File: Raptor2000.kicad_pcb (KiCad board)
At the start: 4 copper layers, 63.5 x 76.2 mm, 77 parts, among them J301 ET60T-000-3-08-D04-x-R1-S-x, J501 USB_B_Micro, SW401 RST_SW, U201 IS42S16400J-xC, U202 TC58CVG2S0HRAIG, U401 TM4C1294NCPDTGOOD, U501 FT232RL, Y401 Crystal_GND24, Y402 Crystal

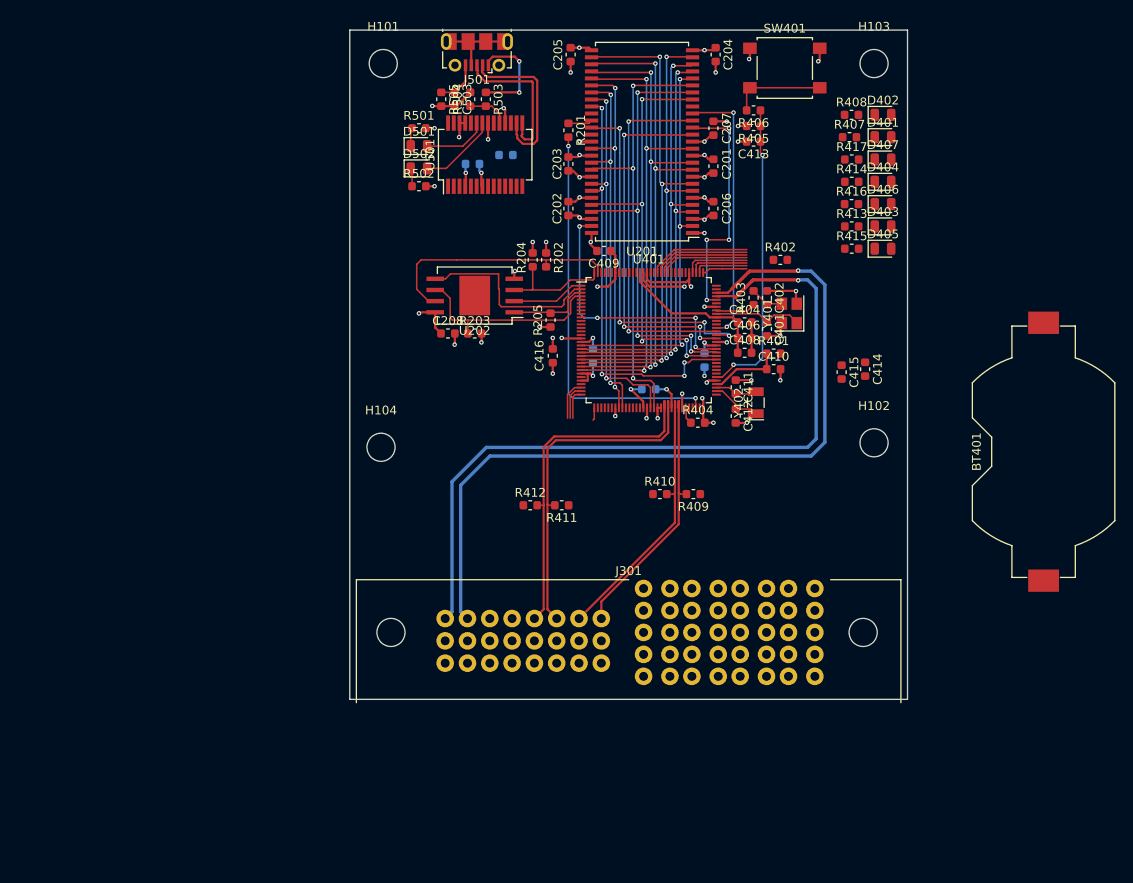
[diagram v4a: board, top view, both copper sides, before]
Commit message: replaced battery with ldo connected to external vbatt. Layout passes DRC
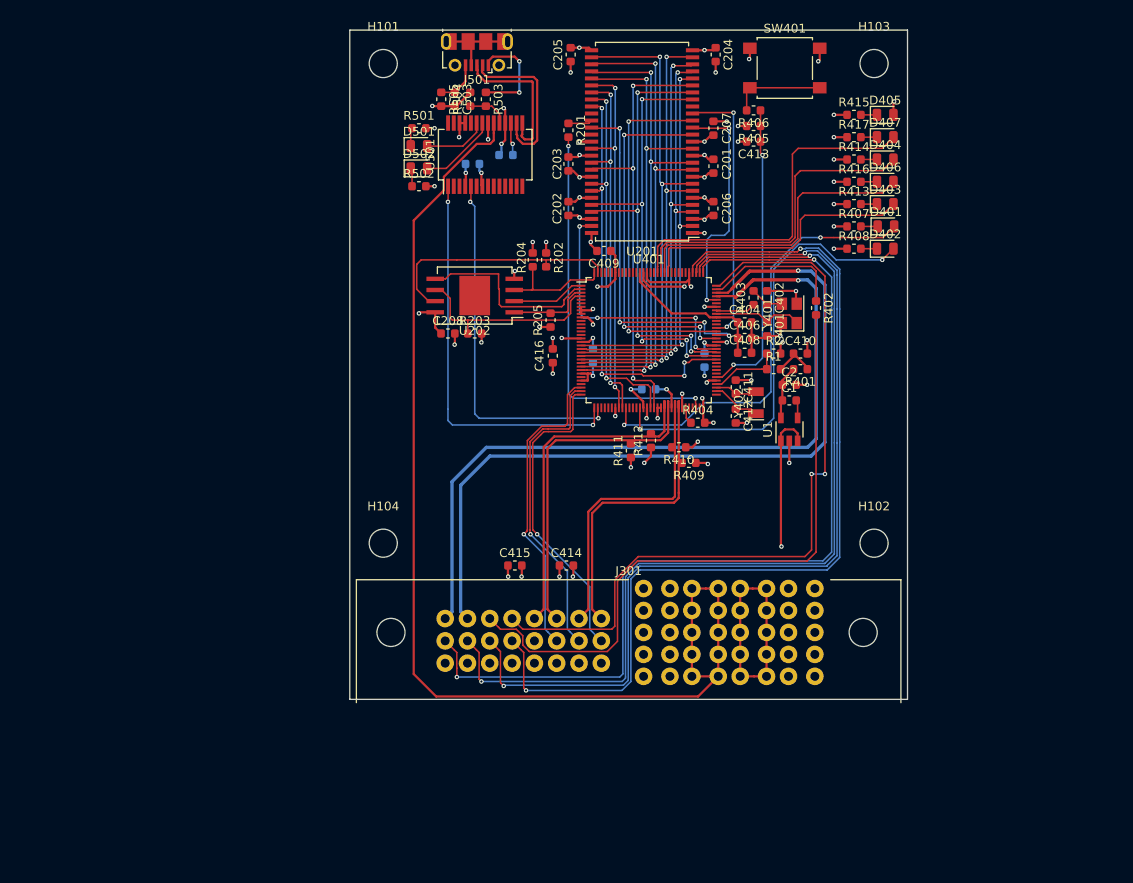
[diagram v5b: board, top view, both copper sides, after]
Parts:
- removed BT401: Battery_Cell, Battery:BatteryHolder_Keystone_1058_1x2032
- added C1: 0.1u, Capacitor_SMD:C_0603_1608Metric, F.Cu at (177.0, 93.0)
- added C2: 10u, Capacitor_SMD:C_0603_1608Metric, F.Cu at (177.0, 91.2)
- added R1: 0, Capacitor_SMD:C_0603_1608Metric, F.Cu at (175.3, 89.4)
- added R2: DNP, Capacitor_SMD:C_0603_1608Metric, F.Cu at (175.3, 87.6)
- added U1: LT1761-3, Package_TO_SOT_SMD:TSOT-23-5, F.Cu at (177.0, 96.3)
- moved C415 43.2 mm to (145.8, 111.8), turned to 0 degrees
- moved C414 40.7 mm to (151.7, 111.8), turned to 0 degrees
- moved R412 15.6 mm to (161.3, 97.5), turned to 90 degrees
- moved R408 15.2 mm to (184.4, 75.7)
- moved D402 15.2 mm to (188.0, 75.7)
- moved D405 15.2 mm to (188.0, 60.5)
- moved R415 15.2 mm to (184.4, 60.5)
- moved H102 11.4 mm to (186.7, 109.2)
- moved H104 10.9 mm to (130.8, 109.2)
- moved R407 10.2 mm to (184.4, 73.2)
- moved D401 10.2 mm to (188.0, 73.2)
- moved R411 10.0 mm to (159.0, 98.7), turned to 90 degrees
- moved R402 6.82 mm to (180.1, 82.4), turned to 270 degrees
- moved R410 5.75 mm to (164.5, 98.3), turned to 180 degrees
- moved R409 3.59 mm to (165.6, 100.1)
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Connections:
- U401 pad 68: /TM4C129/VBat -> /TM4C129/VBat_R
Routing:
- net +5V: track 0.00 -> 130.1 mm
- net /Connectors/JTAG_TDO: track 5.15 -> 107.6 mm, vias 0 -> 2
- net /Connectors/JTAG_TDI: track 6.10 -> 107.8 mm, vias 0 -> 2
- net /Connectors/JTAG_TMS: track 6.75 -> 107.7 mm, vias 0 -> 2
- net /Connectors/JTAG_TCK: track 7.40 -> 107.3 mm, vias 0 -> 2
- net /Connectors/USB_OTG_VBUS: track 0.00 -> 88.2 mm, vias 0 -> 2
- net /TM4C129/USB_ID: track 0.00 -> 75.0 mm
- net /TM4C129/ETH_LED1: track 0.00 -> 51.3 mm, vias 0 -> 2
- net /TM4C129/ETH_LED0: track 0.00 -> 50.4 mm, vias 0 -> 2
- net +BATT: track 0.00 -> 47.5 mm, vias 0 -> 1
- net /TM4C129/UART_DEBUG_RXD: track 1.47 -> 45.4 mm, vias 0 -> 2
- net /TM4C129/UART_DEBUG_TXD: track 0.00 -> 41.7 mm, vias 0 -> 2
- net /Connectors/~INHIBIT: track 3.47 -> 35.7 mm, vias 0 -> 1
- net /Connectors/~ENABLE: track 4.02 -> 35.3 mm, vias 0 -> 1
- net /Connectors/~SYSRESET: track 4.56 -> 35.1 mm, vias 0 -> 1
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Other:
- net class USB: trace_width 0.254 -> 0.1778

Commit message: moved ldo vbatt circuit to a sheet
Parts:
- removed R401: 51, Resistor_SMD:R_0603_1608Metric
- added R3: 51, Resistor_SMD:R_0603_1608Metric, F.Cu at (178.3, 89.4)
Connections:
- net /TM4C129/Batt_Pos renamed /TM4C129/V_Batt/Vout

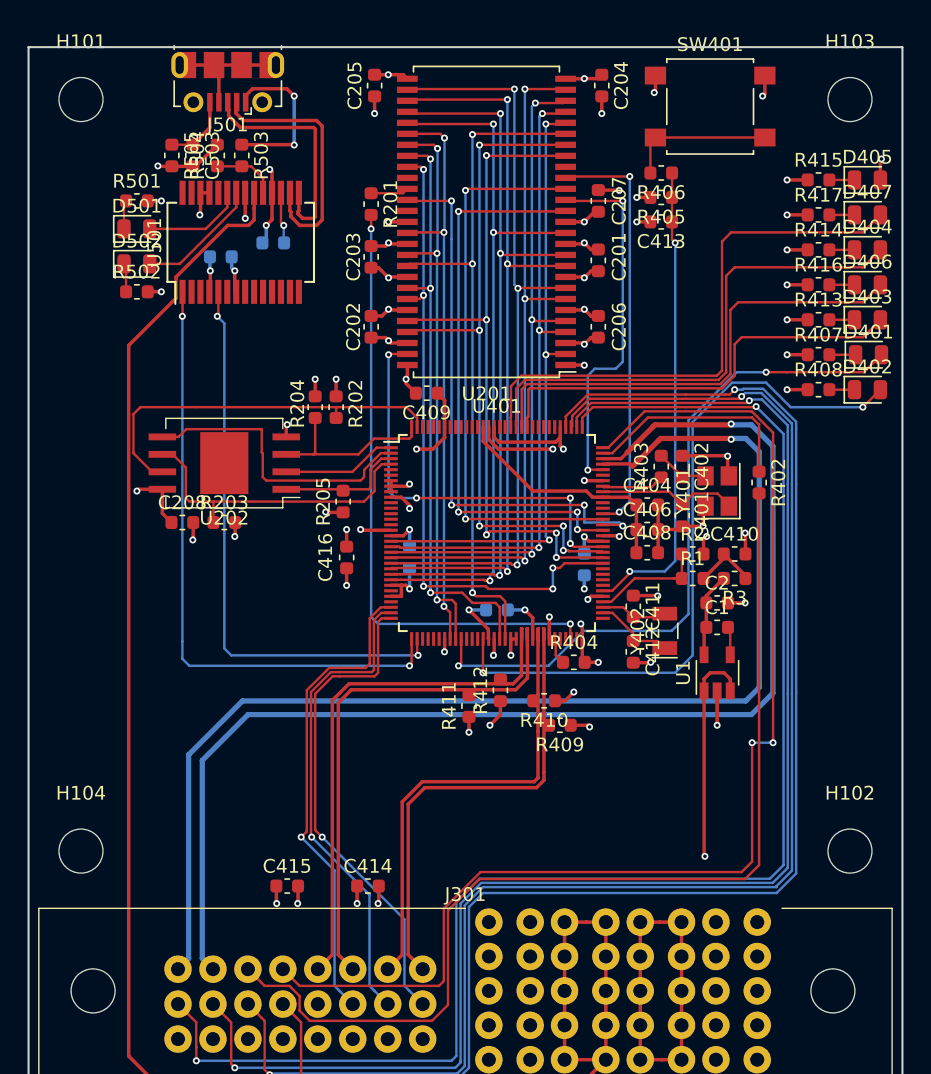
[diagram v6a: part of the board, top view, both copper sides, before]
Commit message: removed rc filter on vbatt output. Included ltspice sim to prove it's unneeded.
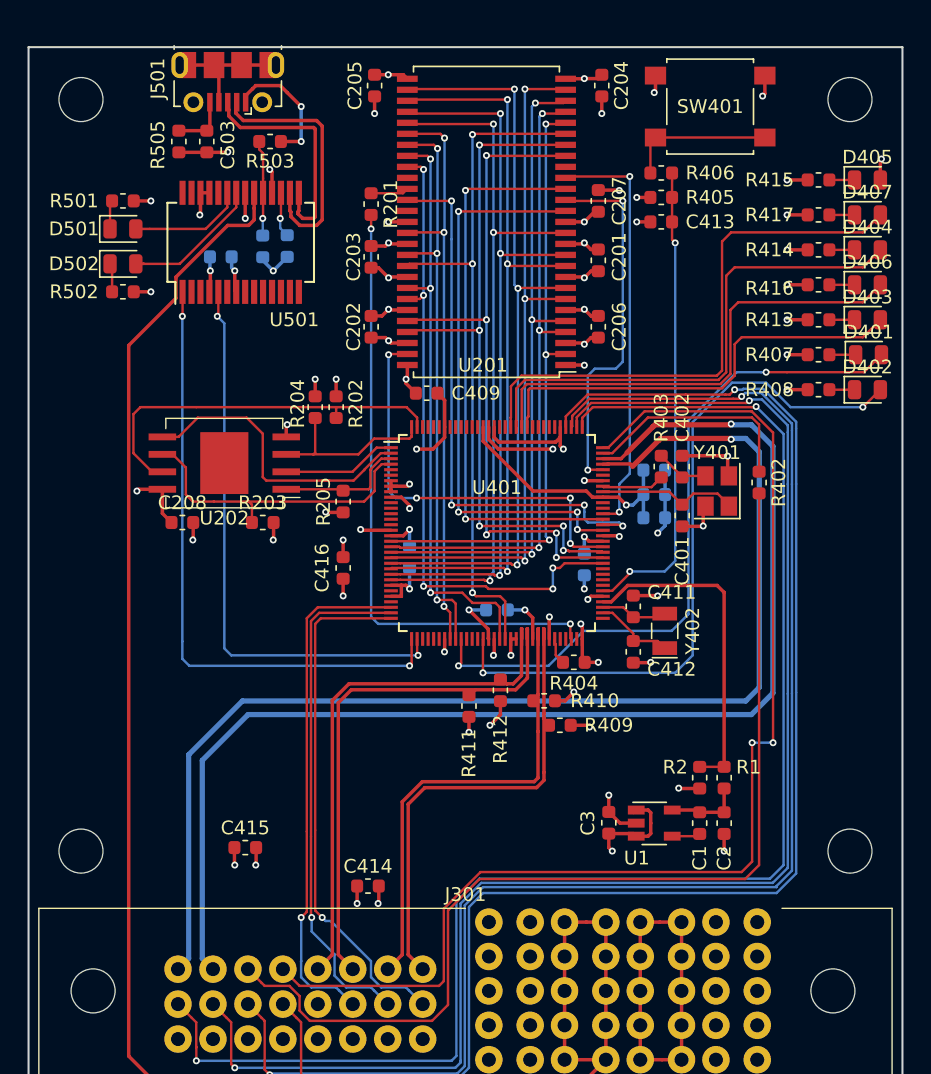
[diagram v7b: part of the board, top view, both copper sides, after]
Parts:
- removed C410: 0.1u, Capacitor_SMD:C_0603_1608Metric
- removed R3: 51, Resistor_SMD:R_0603_1608Metric
- added C3: 1u, Capacitor_SMD:C_0603_1608Metric, F.Cu at (169.2, 107.2)
- C1: value 0.1u -> 0.01u
- C404, C406, C408, R504: moved to B.Cu
- R1: value 0 -> DNP
- R2: value DNP -> 0
- moved R2 16.3 mm to (175.8, 103.9), turned to 270 degrees
- moved C2 16.0 mm to (177.5, 107.2), turned to 270 degrees
- moved R1 14.7 mm to (177.5, 103.9), turned to 270 degrees
- moved C1 14.3 mm to (175.8, 107.2), turned to 270 degrees
- moved U1 11.8 mm to (172.5, 107.2), turned to 0 degrees
- moved R504 7.38 mm to (144.0, 65.3), turned to 270 degrees
- moved C415 4.13 mm to (142.7, 109.0)
- moved R203 2.79 mm to (144.0, 85.3)
- moved C406 2.59 mm to (172.5, 83.3)
- moved C404 2.59 mm to (172.5, 81.5)
- moved C408 2.59 mm to (172.5, 85.0)
- moved R503 2.29 mm to (144.6, 57.7), turned to 180 degrees
- moved C503 1.44 mm to (140.0, 57.7)
- moved R505 1.14 mm to (137.9, 57.7)
- moved C502 1.04 mm to (145.8, 65.3), turned to 270 degrees
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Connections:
- R1 pad 2: /TM4C129/VBat -> /TM4C129/V_Batt/Vout
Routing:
- net /TM4C129/VBat_R: track 8.22 -> 24.0 mm
- net +BATT: track 47.5 -> 39.5 mm
- net /TM4C129/VBat: track 5.11 -> 0.00 mm
- net GND: track 115.5 -> 112.2 mm
- net /USB_to_UART/DBG_VBUS: track 11.8 -> 9.46 mm
- net Net-(R503-Pad2): track 4.74 -> 6.96 mm, vias 0 -> 1
- net /Connectors/~SYSRESET: track 35.1 -> 37.3 mm
- net /Connectors/~INHIBIT: track 35.7 -> 37.8 mm
- net /Connectors/~ENABLE: track 35.3 -> 37.3 mm
- net /USB_to_UART/USB_LED_1: track 9.04 -> 10.6 mm
- net /USB_to_UART/USB_LED_0: track 7.33 -> 8.35 mm
- net /USB_to_UART/DBG_USB_SHIELD: track 5.12 -> 4.19 mm
- net /TM4C129/VDDC: track 17.6 -> 18.4 mm, vias 0 -> 1
- net /TM4C129/V_Batt/Vout: track 6.14 -> 5.56 mm

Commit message: sourced all parts, except LEDs. added bom. fixed a few footprints/values.
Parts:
- D501, D502: footprint Diode_SMD:D_0805_2012Metric -> LED_SMD:LED_0805_2012Metric
- R1, R2: footprint Capacitor_SMD:C_0603_1608Metric -> Resistor_SMD:R_0603_1608Metric
